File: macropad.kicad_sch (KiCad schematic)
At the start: 7 parts, among them SW1 SW_Push, SW2 SW_Push, SW3 SW_Push, SW4 SW_Push, SW5 SW_Push, SW6 SW_Push

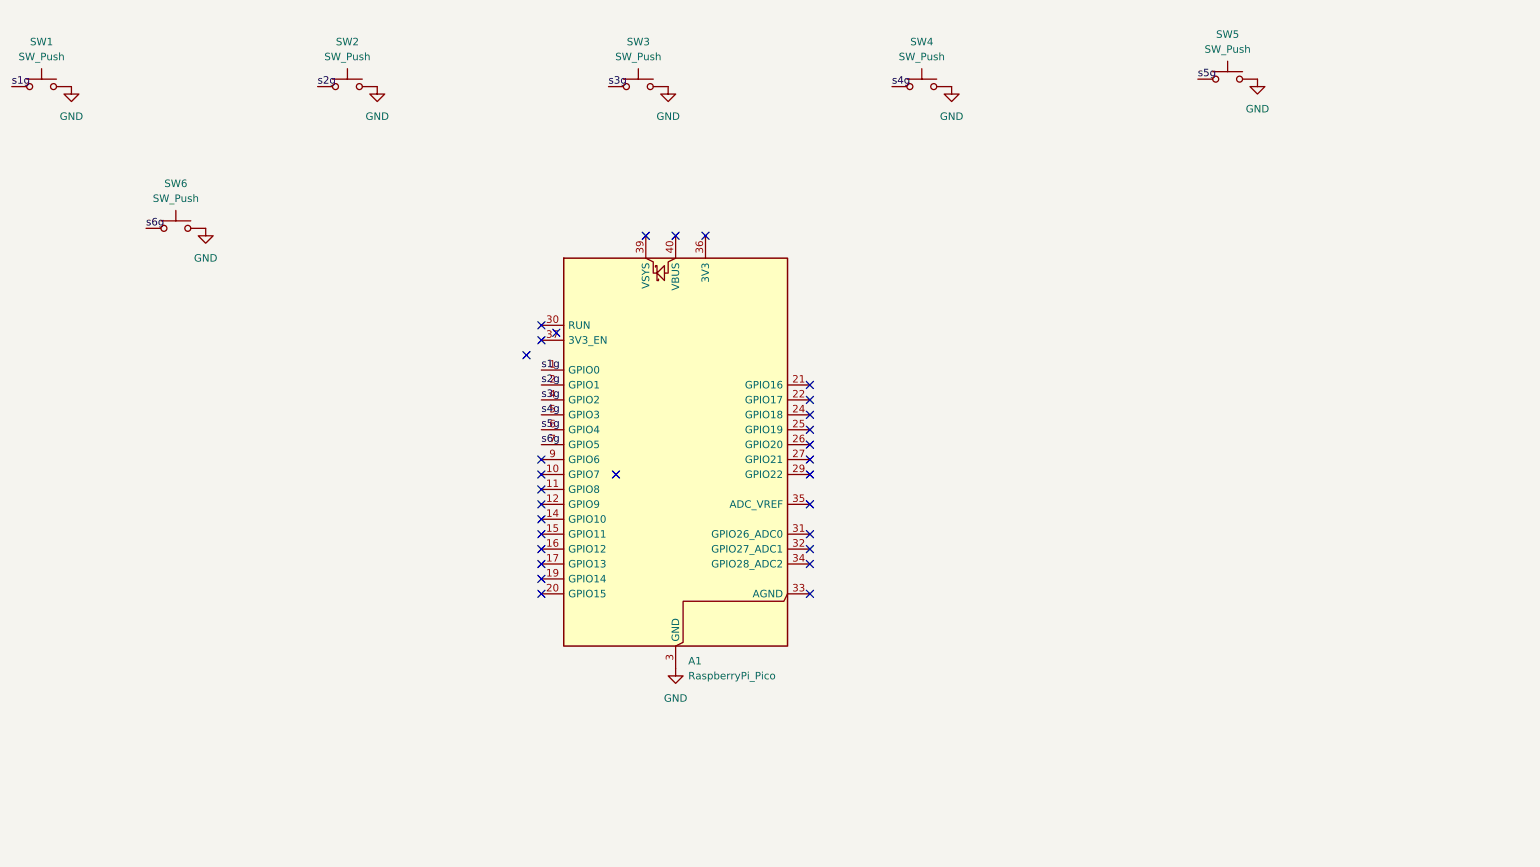
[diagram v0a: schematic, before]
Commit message: Added some text in the silkscreen
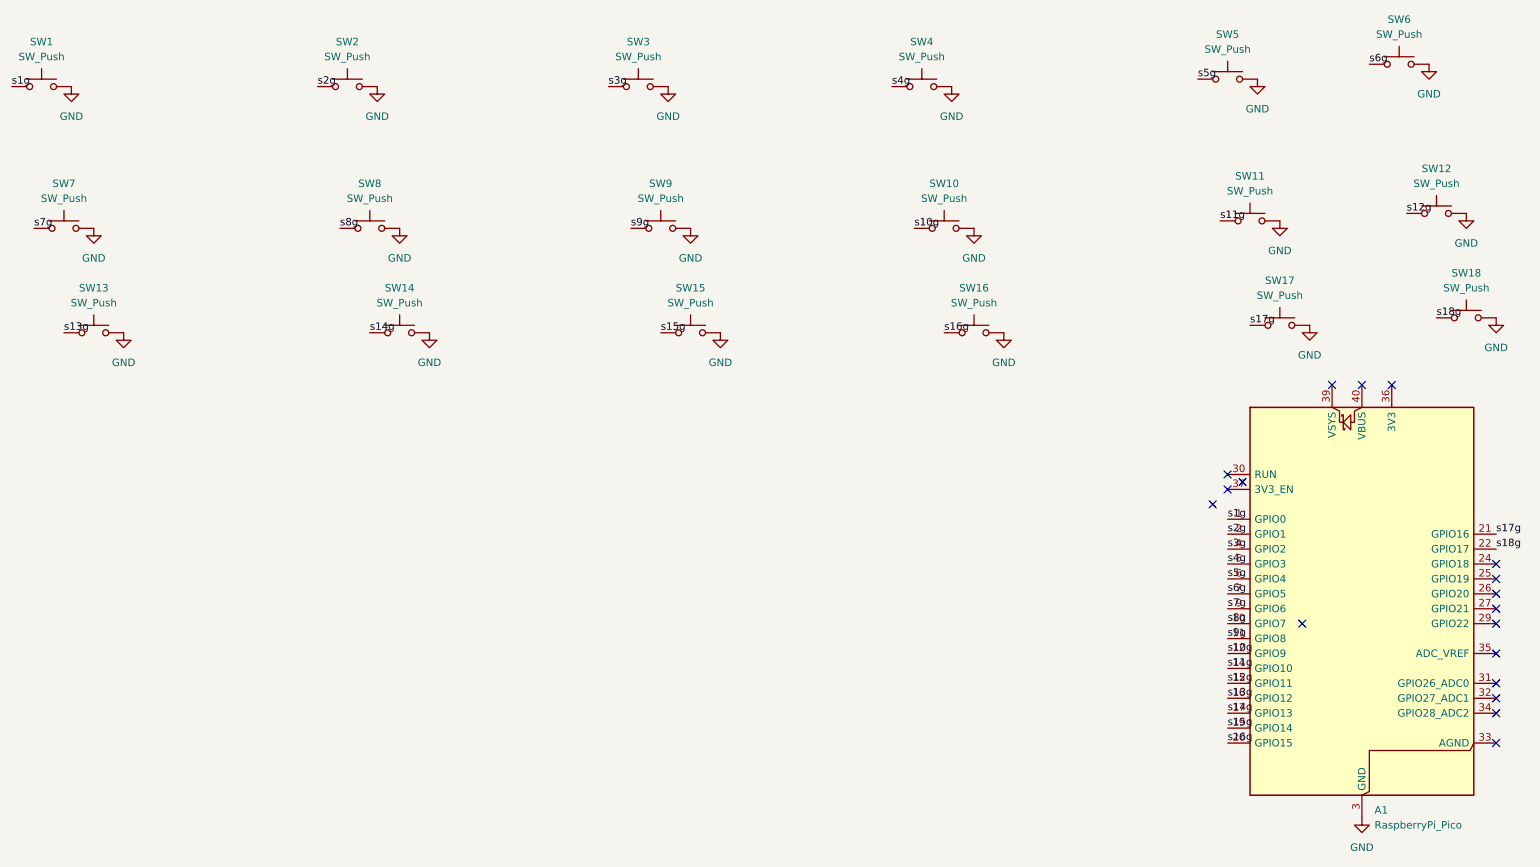
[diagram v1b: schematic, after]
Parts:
- added SW10, SW11, SW12, SW13, SW14, SW15, SW16, SW17, SW18, SW7, SW8, SW9: SW_Push, Button_Switch_Keyboard:SW_Cherry_MX_1.00u_PCB, symbol Switch:SW_Push
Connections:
- net GND: now also SW10.2, SW11.2, SW12.2, SW13.2, SW14.2, SW15.2, SW16.2, SW17.2, SW18.2, SW7.2, SW8.2, SW9.2
- net s8g: now reaches A1.10 (GPIO7)
- net s8g: now also SW8.1
- net s9g: now reaches A1.11 (GPIO8)
- net s9g: now also SW9.1
- net s10g: now reaches A1.12 (GPIO9)
- net s10g: now also SW10.1
- net s11g: now reaches A1.14 (GPIO10)
- net s11g: now also SW11.1
- net s12g: now reaches A1.15 (GPIO11)
- net s12g: now also SW12.1
- net s13g: now reaches A1.16 (GPIO12)
- net s13g: now also SW13.1
- net s14g: now reaches A1.17 (GPIO13)
- net s14g: now also SW14.1
- net s15g: now reaches A1.19 (GPIO14)
- net s15g: now also SW15.1
- net s16g: now reaches A1.20 (GPIO15)
- net s16g: now also SW16.1
- net s17g: now reaches A1.21 (GPIO16)
- net s17g: now also SW17.1
- net s18g: now reaches A1.22 (GPIO17)
- net s18g: now also SW18.1
- net s7g: now reaches A1.9 (GPIO6)
- net s7g: now also SW7.1
- no-connect marks 30 -> 18
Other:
- moved on the sheet: A1, SW6
